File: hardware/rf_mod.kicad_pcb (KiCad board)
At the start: 4 copper layers, 100 x 100 mm, 162 parts, among them J1001 SMA, J1002 SMA, J1003 Pmod, J101 SMA, J102 SMA, J103 SMA, J1101 SMA, J1102 SMA, J1201 SMA, J1202 SMA, J201 SMA, J202 SMA, J401 SMA, J402 SMA, J501 SMA, J502 SMA, J701 SMA, J702 SMA, J703 SMA, J801 SMA, J802 SMA, J803 SMA, J901 USB-C, J902 SMA, Q1001 AO3401A, Q1101 AO3401A, Q1201 AO3401A, Q501 AO3401A, Q701 AO3401A, Q801 AO3401A, SW1001 ON, SW1101 ON, SW1201 ON, SW501 ON, SW701 ON, SW801 ON, U1001 3.3V, U1002 MAX2871, U1101 3.3V, U1102 MAX2871, U1201 GALI-84+, U501 GALI-84+, U701 3.3V, U702 ADL5350, U801 3.3V, U802 ADL5350, U901 MT3608, U902 3.3V, U903 74LVC1G17, X901 25 MHz

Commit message: Jacks in a checkerboard on every board (Prompt 12): every pair 14.85 mm or more
IN at a cell's top-left slot, OUT at its bottom-right, a two-cell tile's third jack
at its right cell's top-left.  geometry.py now asserts 14.3 mm between every pair.

- AMOD-P: all thirteen tiles re-laid; P8's crystal and P9's resonator at 45 degrees
  (P8's jacks 0.5 mm further out, slots TLo/BRo); P11's taps on TL/BR slots.
- AMOD-A: A2-A4 share opa_tile_br; A4's OPA847 now SOT-23-6 (C160422); A7 now
  Nexperia's 74HC4046APW-Q100J in TSSOP-16 (C546981, 234 in stock); A8, A9 and A11
  re-laid with OUT at the bottom-right; the back's QR code moved.  $50.90 of parts.
- RF-MOD: the mixers' LO jacks moved from the top middle to TL1.
- Assembler's notes say the 45-degree parts are meant; PLAN, DOA, review brief,
  README and the chat log updated.

All three boards: ERC 0, DRC 0, every fab check passed.

Co-Authored-By: Claude Opus 5.5 <noreply@anthropic.com>
Claude-Session: https://claude.ai/code/session_01RKeoKvFFzjk3cEBLCXXHnB
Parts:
- moved J702 1.75 mm to (34.0, 55.5)
- moved J802 1.75 mm to (77.0, 55.5)
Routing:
- net /R8_LOJ: track 10.9 -> 12.6 mm
- net /R7_LOJ: track 10.9 -> 12.6 mm
- net GND: vias 274 -> 280

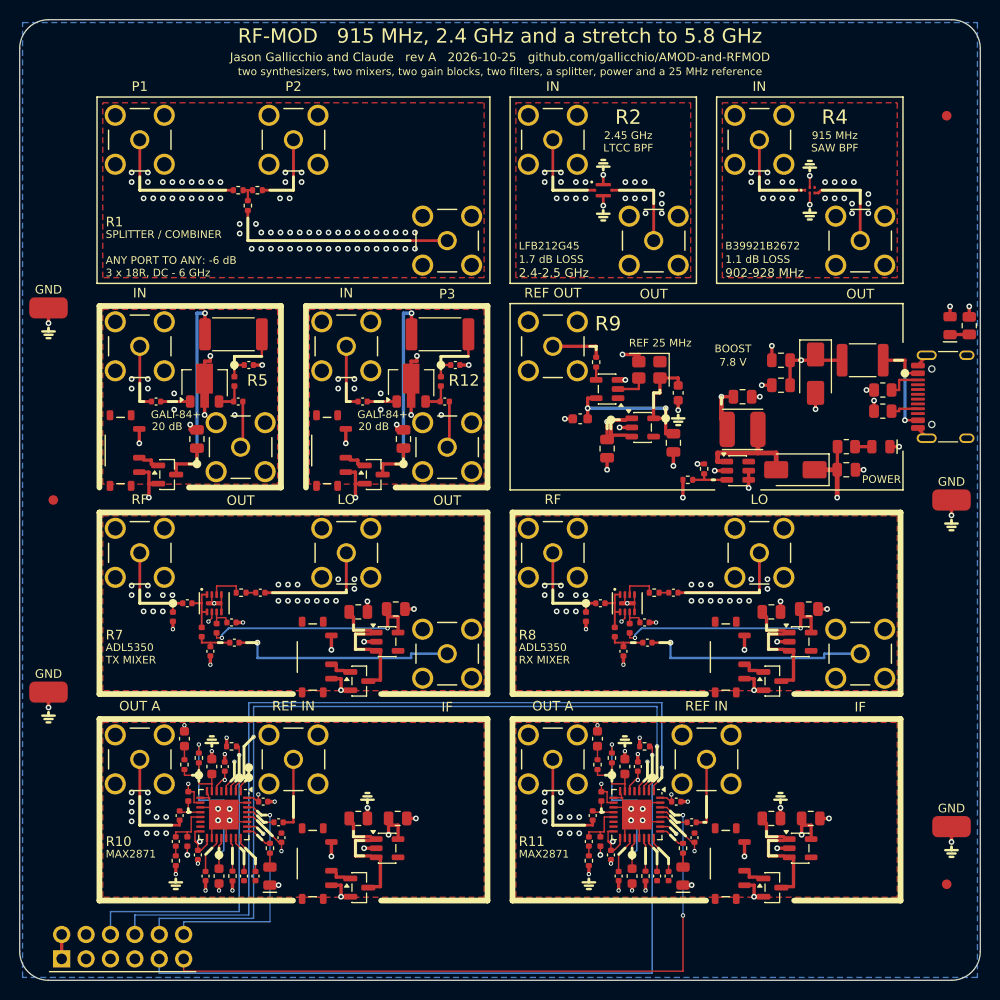
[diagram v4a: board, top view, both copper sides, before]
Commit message: RF-MOD rev A: the QPL9547 LNA in R5 and the TRF3722 quadrature transmitter as R13 (Prompt 13)
- R5: QPL9547TR7 (C5367093, 5,070 in stock; rev A's search had missed the reel) on
  Qorvo's evaluation circuit, in place of a second GALI-84+: 0.3 dB of noise figure
  for every receiver.  R12 stays the GALI-84+ gain block; the 7.8 V strip now ends at it.
- R13 (cells of the old R11): TRF3722 (C1850395, 2,218) with I and Q from the ECP5
  board's two DACs through resistor networks to its 0.25 V common mode, TI's
  fractional loop filter, a TLV75733 in the WSON (0.56 W) on a 3.3 V island, the
  reference from R10's REF IN on the back, SPI shared with R10 (LE IO6, readback IO5).
  Jason's "Yes. Add that tile." from Appendix D's questions.
- The second MAX2871 (R11) is gone: R13 has its own PLL and VCO.
- Symbols: stacked hidden pins for the TRF3722's grounds; the generic schematic block
  closes up its rows when they would reach the notes.  A DFN-8 stand-in 3D body.
- PLAN_LEVEL2.md: the plan for AMOD-2 and RF-MOD-2 and the first level checked again.

RF-MOD: ERC 0, DRC 0, every fab check passed, $57.18 of parts a board.

Co-Authored-By: Claude Opus 5.5 <noreply@anthropic.com>
Claude-Session: https://claude.ai/code/session_01RKeoKvFFzjk3cEBLCXXHnB
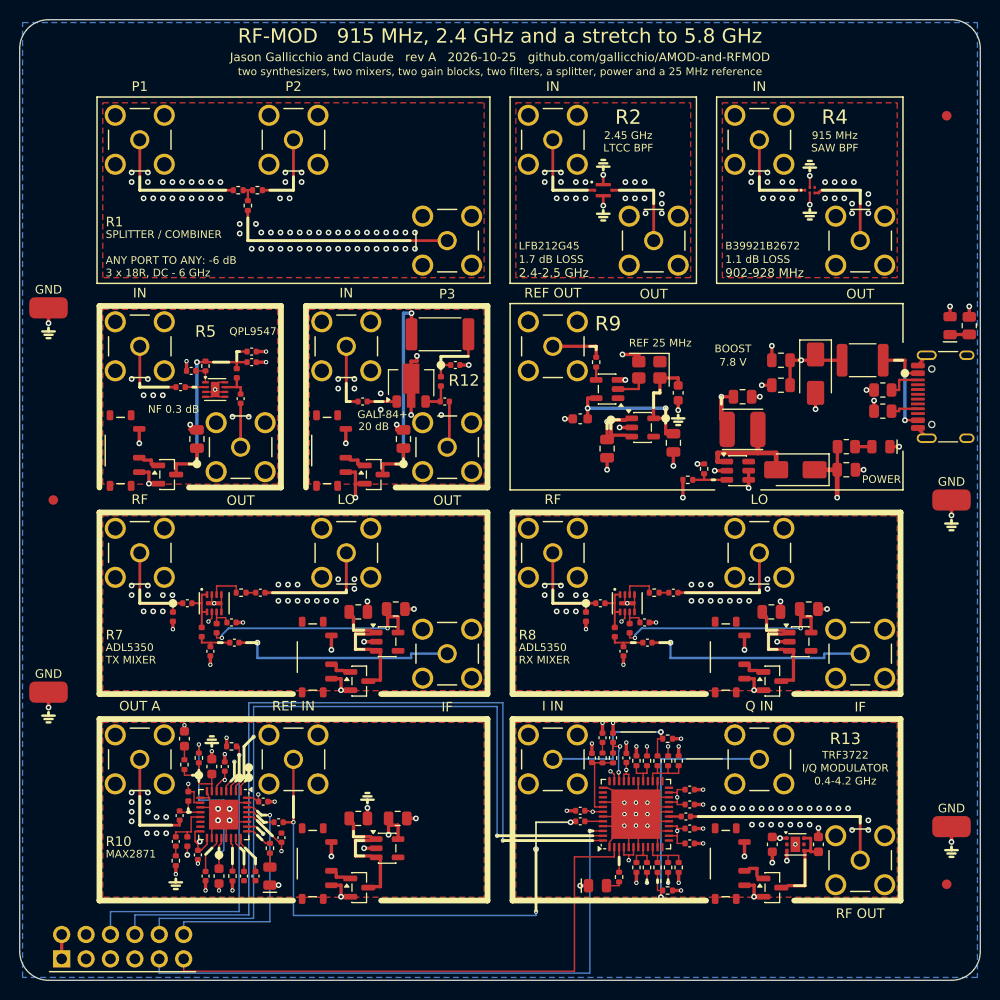
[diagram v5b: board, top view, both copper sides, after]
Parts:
- removed C1101, C1102: 1u, Capacitor_SMD:C_0805_2012Metric
- removed C1103: 470p, Capacitor_SMD:C_0603_1608Metric
- removed C1104: 6.8n, Capacitor_SMD:C_0603_1608Metric
- removed C1105, C1106, C1107, C1108, C1111: 100n, Capacitor_SMD:C_0402_1005Metric
- removed C1109, C1110: 100p, Capacitor_SMD:C_0402_1005Metric
- removed C1112, C1114, C1115: 1u, Capacitor_SMD:C_0402_1005Metric
- removed C1113: 100p, Capacitor_SMD:C_0603_1608Metric
- removed J1101, J1102: SMA, amod:SMA_BWSMA-KE-Z001_Vertical
- removed L1101, L1102: 27n, Inductor_SMD:L_0402_1005Metric
- removed LED1101: LOCK, amod:LED_0805_2012Metric_Kbar
- removed Q1101: AO3401A, Package_TO_SOT_SMD:SOT-23
- removed R1101: 470, Resistor_SMD:R_0402_1005Metric
- removed R1102: 820, Resistor_SMD:R_0402_1005Metric
- removed R1103: 100k, Resistor_SMD:R_0402_1005Metric
- removed R1104: 1k, Resistor_SMD:R_0402_1005Metric
- removed R1105: 51R, Resistor_SMD:R_0402_1005Metric
- removed R1106: 5.1k, Resistor_SMD:R_0402_1005Metric
- removed SW1101: ON, amod:SW_SPDT_Shouhan_MSK12C02
- removed U1101: 3.3V, Package_TO_SOT_SMD:SOT-23-5
- removed U1102: MAX2871, Package_DFN_QFN:QFN-32-1EP_5x5mm_P0.5mm_EP3.1x3.1mm
- added C1301: 100n, Capacitor_SMD:C_0402_1005Metric, F.Cu at (69.8, 80.2)
- added C1302: 100p, Capacitor_SMD:C_0402_1005Metric, F.Cu at (69.8, 81.7)
- added C1303: 100p, Capacitor_SMD:C_0402_1005Metric, F.Cu at (69.8, 84.2)
- added C1304: 100n, Capacitor_SMD:C_0402_1005Metric, F.Cu at (69.8, 85.8)
- added C1305: 4.7p, Capacitor_SMD:C_0402_1005Metric, F.Cu at (69.3, 83.0)
- added C1306: 100n, Capacitor_SMD:C_0402_1005Metric, F.Cu at (58.4, 82.3)
- added C1307: 100n, Capacitor_SMD:C_0402_1005Metric, F.Cu at (63.1, 76.8)
- added C1308: 1n, Capacitor_SMD:C_0402_1005Metric, F.Cu at (59.6, 76.8)
- added C1309: 10n, Capacitor_SMD:C_0402_1005Metric, F.Cu at (60.7, 74.8)
- added C1310: 330p, Capacitor_SMD:C_0402_1005Metric, F.Cu at (61.8, 74.8)
- added C1311: 100n, Capacitor_SMD:C_0402_1005Metric, F.Cu at (58.4, 83.5)
- added C1312: 1u, Capacitor_SMD:C_0603_1608Metric, F.Cu at (83.2, 85.8)
- added C1313: 1u, Capacitor_SMD:C_0603_1608Metric, F.Cu at (78.3, 85.8)
- added C505: 100p, Capacitor_SMD:C_0402_1005Metric, F.Cu at (17.9, 36.6)
- added C506: 10u, Capacitor_SMD:C_0805_2012Metric, F.Cu at (18.4, 43.6)
- added J1301: SMA, amod:SMA_BWSMA-KE-Z001_Vertical, F.Cu at (55.5, 77.0)
- added J1302: SMA, amod:SMA_BWSMA-KE-Z001_Vertical, F.Cu at (77.0, 77.0)
- added J1303: SMA, amod:SMA_BWSMA-KE-Z001_Vertical, F.Cu at (87.5, 87.5)
- added LED1301: LOCK, amod:LED_0805_2012Metric_Kbar, F.Cu at (60.1, 90.2)
- added Q1301: AO3401A, Package_TO_SOT_SMD:SOT-23, F.Cu at (78.3, 90.3)
- added R1301: 1.1k, Resistor_SMD:R_0402_1005Metric, F.Cu at (60.7, 76.8)
- added R1302: 1.1k, Resistor_SMD:R_0402_1005Metric, F.Cu at (61.8, 76.8)
- added R1303: 75, Resistor_SMD:R_0402_1005Metric, F.Cu at (64.2, 77.2)
- added R1304: 910, Resistor_SMD:R_0402_1005Metric, F.Cu at (65.3, 77.2)
- added R1305: 270, Resistor_SMD:R_0402_1005Metric, F.Cu at (66.4, 77.2)
- added R1306: 910, Resistor_SMD:R_0402_1005Metric, F.Cu at (67.5, 77.2)
- added R1307: 100, Resistor_SMD:R_0402_1005Metric, F.Cu at (68.6, 77.2)
- added R1308: 56, Resistor_SMD:R_0402_1005Metric, F.Cu at (67.5, 74.8)
- added R1309: 75, Resistor_SMD:R_0402_1005Metric, F.Cu at (64.2, 88.2)
- added R1310: 910, Resistor_SMD:R_0402_1005Metric, F.Cu at (65.3, 88.2)
- added R1311: 270, Resistor_SMD:R_0402_1005Metric, F.Cu at (66.4, 88.2)
- added R1312: 910, Resistor_SMD:R_0402_1005Metric, F.Cu at (67.5, 88.2)
- added R1313: 100, Resistor_SMD:R_0402_1005Metric, F.Cu at (68.6, 88.2)
- added R1314: 56, Resistor_SMD:R_0402_1005Metric, F.Cu at (67.5, 90.7)
- added R1315: 1k, Resistor_SMD:R_0402_1005Metric, F.Cu at (62.4, 89.2)
- added SW1301: ON, amod:SW_SPDT_Shouhan_MSK12C02, F.Cu at (73.5, 87.8)
- added U1301: TRF3722, Package_DFN_QFN:Texas_RGZ0048A_VQFN-48-1EP_7x7mm_P0.5mm_EP5.15x5.15mm, F.Cu at (64.2, 82.7)
- added U1302: 3.3V, Package_SON:WSON-6-1EP_2x2mm_P0.65mm_EP1x1.6mm, F.Cu at (80.8, 85.8)
- C504: value 10u -> 1u; footprint Capacitor_SMD:C_0805_2012Metric -> Capacitor_SMD:C_0402_1005Metric
- L501: value 27n -> 18n
- R501: value 22R -> 3.3k; footprint Resistor_SMD:R_2512_6332Metric -> Resistor_SMD:R_0402_1005Metric
- U501: value GALI-84+ -> QPL9547; footprint Package_TO_SOT_SMD:SOT-89-3 -> Package_DFN_QFN:DFN-8-1EP_2x2mm_P0.5mm_EP0.9x1.6mm
- moved C504 10.7 mm to (24.1, 34.5), turned to 0 degrees
- moved R501 4.40 mm to (19.3, 36.0), turned to 90 degrees
- moved C501 2.96 mm to (16.8, 38.2)
- moved U501 1.30 mm to (20.4, 38.5), turned to 0 degrees
- moved L501 0.89 mm to (22.6, 36.8)
- moved C503 0.42 mm to (24.1, 35.6)
- moved C502 0.39 mm to (23.0, 39.5), turned to -90 degrees
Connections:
- net /R10_REF renamed /REF25
- C503 pad 1: /R5_VD -> /R5_VS
- C504 pad 1: GND -> /R5_VS
- C504 pad 2: /R5_VS -> GND
- L501 pad 1: /R5_VD -> /R5_VS
- Q501 pad 2: +8V -> +5V
- R501 pad 1: /R5_VS -> /R5_VB
- R501 pad 2: /R5_VD -> /R5_VS
- SW501 pad 3: +8V -> +5V
- U501 pad 1: /R5_IN_A -> /R5_VB
- U501 pad 2: GND -> /R5_IN_A
- U501 pad 3: /R5_OUT_A -> GND
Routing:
- net /REF25: track 7.62 -> 56.2 mm, vias 0 -> 4
- net /R11_V33: track 29.5 -> 0.00 mm, vias 9 -> 0
- net /R13_BBQ: track 0.00 -> 27.6 mm, vias 0 -> 1
- net /R13_V33: track 0.00 -> 25.6 mm, vias 0 -> 11
- net /R13_RFOUT: track 0.00 -> 22.2 mm
- net GND: track 127.6 -> 149.3 mm, vias 280 -> 305
- net /R11_TN: track 18.5 -> 0.00 mm, vias 2 -> 0
- net /PMOD6: track 80.8 -> 62.5 mm
- net /R13_BBI: track 0.00 -> 16.9 mm, vias 0 -> 1
- net /PMOD5: track 72.2 -> 59.0 mm, vias 2 -> 0
- net /R11_OUTA: track 11.5 -> 0.00 mm
- net /R11_VS: track 11.4 -> 0.00 mm
- net /R13_VS: track 0.00 -> 9.05 mm
- net /R5_VD: track 8.30 -> 0.00 mm
- net /R13_CP: track 0.00 -> 7.65 mm
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- added copper zone on In2.Cu, net /R13_V33
- removed copper zone on In2.Cu, net /R11_V33
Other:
- board text added: "0.4-4.2 GHz"
- board text added: "I IN"
- board text added: "I/Q MODULATOR"
- board text added: "NF 0.3 dB"
- board text added: "Q IN"
- board text added: "QPL9547"
- board text added: "R13"
- board text added: "RF OUT"
- board text added: "TRF3722"
- board text removed: "R11"

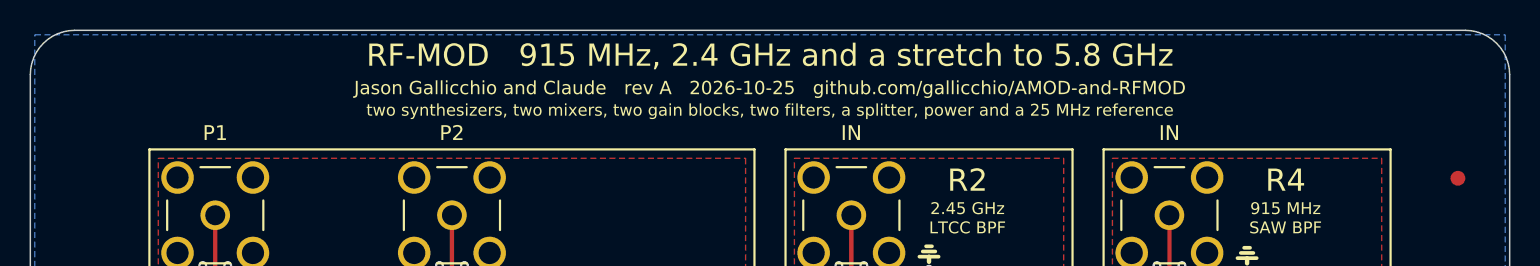
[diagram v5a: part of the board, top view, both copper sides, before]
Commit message: RF-MOD-2 rev A: the coherent I/Q transceiver board (Prompt 13)
Eleven tiles for the ECP5-2ADC-2DAC board: an ADL5375-05 modulator fed by its
DACs (X1), an ADL5380 demodulator with two OPA810 difference amplifiers into its
ADCs (X2), RF-MOD's MAX2871 synthesizer with its own REF IN (X3) split by a
resistive splitter into both LOs (X5), the QPL9547 LNA (X4), an AD8318 log
detector (X6), a switched avalanche noise source with an ADL5611 and a 20 dB
pad (X7), a GNSS front end (bias-T, SAW, MAX2659, SAW: X8), a loop for NV
centres' ODMR with every plane cleared under it (X9), USB-C and -5 V (X10) and
a SKY13370 absorptive SPDT on two Pmod lines (X11).  ERC, DRC and every fab
check pass; parts $98.61 a board.  ADL5380's 14 in stock is recorded as Jason's
accepted exception in parts.py and check_outputs reports it.

Generators: per-tile copper voids; hidden stacked symbol pins are passive (a
hidden power input made a global net of its name); schematic chips spaced by
their labels' widths and wrapped; the result note's real height sizes the
part rows; synth_tile can carry REF IN at BR1 and extra Pmod pads.

Co-Authored-By: Claude Opus 5.5 <noreply@anthropic.com>
Claude-Session: https://claude.ai/code/session_01RKeoKvFFzjk3cEBLCXXHnB
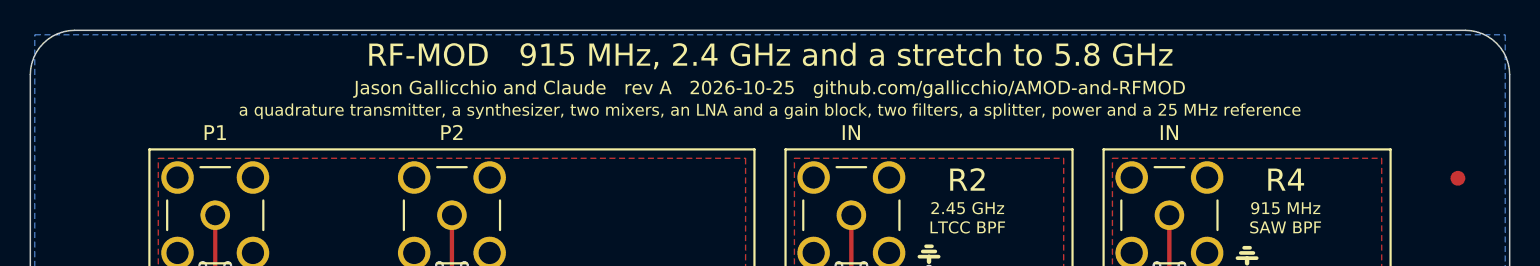
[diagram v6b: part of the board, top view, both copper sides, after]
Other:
- board text added: "a quadrature transmitter, a synthesizer, two mixers, an LNA and a gain block, two filters, a splitter, power and a 25 MHz reference"
- board text removed: "two synthesizers, two mixers, two gain blocks, two filters, a splitter, power and a 25 MHz reference"
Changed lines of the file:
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@@
 		)
 	)
-	(gr_text "two synthesizers, two mixers, two gain blocks, two filters, a splitter, power and a 25 MHz reference"
+	(gr_text "a quadrature transmitter, a synthesizer, two mixers, an LNA and a gain block, two filters, a splitter, power and a 25 MHz reference"
 		(at 50 5.4 0)
 		(layer "F.SilkS")
